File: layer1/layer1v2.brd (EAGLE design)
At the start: 17.8 x 48.3 mm, 15 parts, among them U1 microSD, U2 DS3234, U3 MMA8452Q

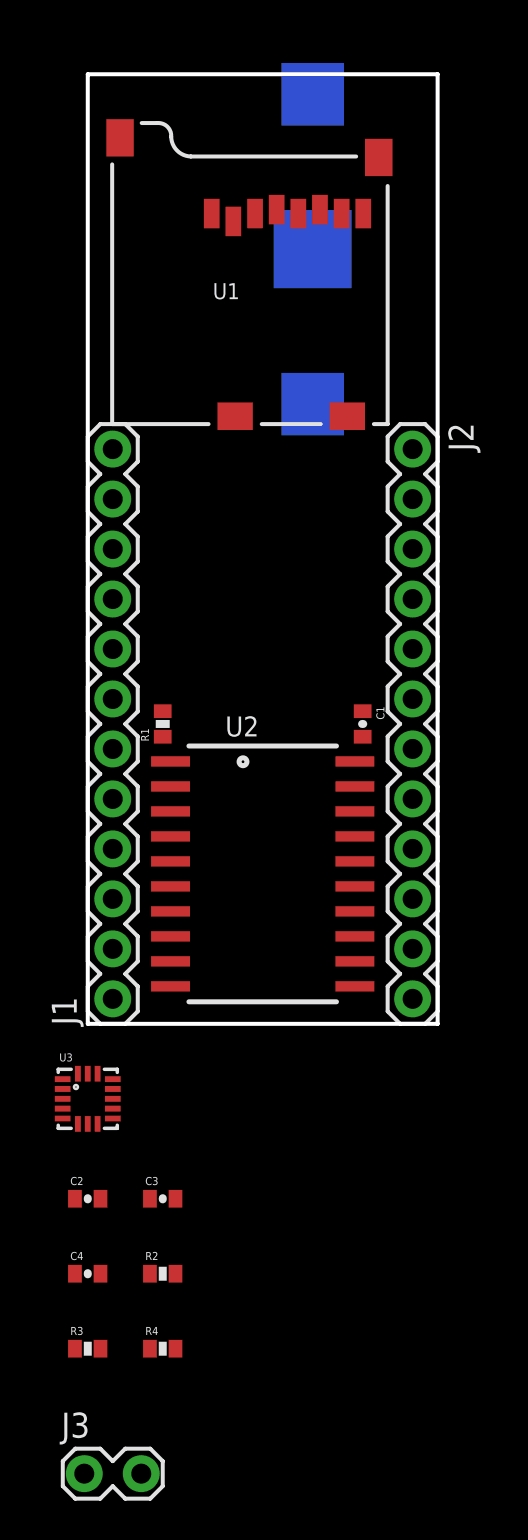
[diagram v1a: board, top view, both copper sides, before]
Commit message: removed battery, add accel
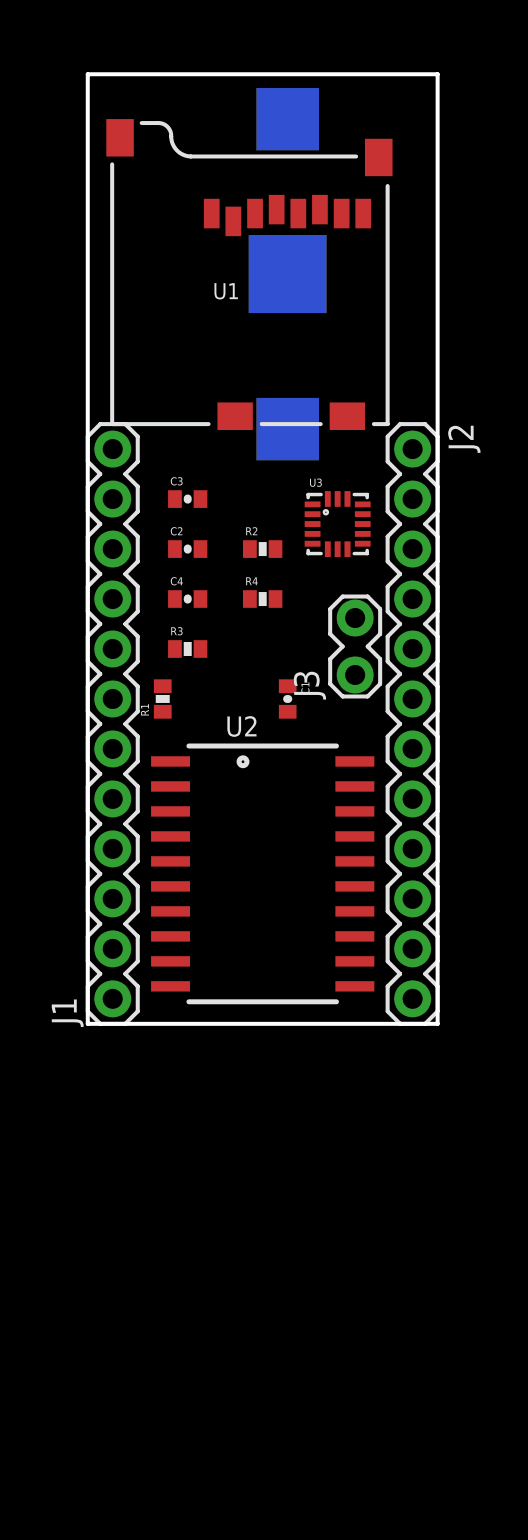
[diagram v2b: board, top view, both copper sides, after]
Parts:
- moved J3 43.0 mm to (13.6, 17.9), turned to 90 degrees
- moved R4 38.4 mm to (8.89, 21.6)
- moved R2 37.2 mm to (8.89, 24.1)
- moved R3 35.9 mm to (5.08, 19.1)
- moved C3 35.6 mm to (5.08, 26.7)
- moved C4 34.7 mm to (5.08, 21.6)
- moved C2 33.4 mm to (5.08, 24.1)
- moved U3 31.9 mm to (12.7, 25.4)
- moved C1 4.02 mm to (10.2, 16.5)
- moved BAT1 1.80 mm to (10.2, 38.1)
- moved R1 1.27 mm to (3.81, 16.5)
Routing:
- added copper zone on layer 16, net GND
- removed copper zone on layer 16, net N$1
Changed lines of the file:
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@@
 </autorouter>
 <elements>
-<element name="BAT1" library="SparkFun" package="BATTCON_12MM_CURVED" value="3V" x="11.43" y="39.37" rot="MR90"/>
-<element name="C1" library="SparkFun" package="0402-CAP" value="22pF" x="13.97" y="15.24" rot="R270"/>
-<element name="R1" library="SparkFun" package="0402-RES" value="10k" x="3.81" y="15.24" rot="R90"/>
+<element name="BAT1" library="SparkFun" package="BATTCON_12MM_CURVED" value="3V" x="10.16" y="38.1" rot="MR90"/>
+<element name="C1" library="SparkFun" package="0402-CAP" value="22pF" x="10.16" y="16.51" rot="R270"/>
+<element name="R1" library="SparkFun" package="0402-RES" value="10k" x="3.81" y="16.51" rot="R90"/>
 <element name="U1" library="SparkFun" package="MICRO-SD-SOCKET-PP" value="microSD" x="15.24" y="30.48"/>
 <element name="U2" library="SparkFun" package="DS3234" value="DS3234" x="8.89" y="7.62" rot="R270"/>
 <element name="J1" library="SparkFun-Connectors" package="1X12" value="" x="1.27" y="1.27" rot="R90"/>
 <element name="J2" library="SparkFun-Connectors" package="1X12" value="" x="16.51" y="29.21" rot="R270"/>
-<element name="U3" library="SparkFun" package="QFN-16_0.5MM" value="MMA8452Q" x="0" y="-3.81"/>
-<element name="C2" library="SparkFun" package="0402-CAP" value="0.1uF" x="0" y="-8.89"/>
-<element name="C3" library="SparkFun" package="0402-CAP" value="0.1uF" x="3.81" y="-8.89"/>
-<element name="C4" library="SparkFun" package="0402-CAP" value="4.7uF" x="0" y="-12.7"/>
-<element name="R2" library="SparkFun" package="0402-RES" value="10k" x="3.81" y="-12.7"/>
-<element name="R3" library="SparkFun" package="0402-RES" value="10k" x="0" y="-16.51"/>
-<element name="R4" library="SparkFun" package="0402-RES" value="10k" x="3.81" y="-16.51"/>
-<element name="J3" library="SparkFun-Connectors" package="1X02_LOCK" value="" x="0" y="-22.86"/>
+<element name="U3" library="SparkFun" package="QFN-16_0.5MM" value="MMA8452Q" x="12.7" y="25.4"/>
+<element name="C2" library="SparkFun" package="0402-CAP" value="0.1uF" x="5.08" y="24.13"/>
+<element name="C3" library="SparkFun" package="0402-CAP" value="0.1uF" x="5.08" y="26.67"/>
+<element name="C4" library="SparkFun" package="0402-CAP" value="4.7uF" x="5.08" y="21.59"/>
+<element name="R2" library="SparkFun" package="0402-RES" value="10k" x="8.89" y="24.13"/>
+<element name="R3" library="SparkFun" package="0402-RES" value="10k" x="5.08" y="19.05"/>
+<element name="R4" library="SparkFun" package="0402-RES" value="10k" x="8.89" y="21.59"/>
+<element name="J3" library="SparkFun-Connectors" package="1X02_LOCK" value="" x="13.589" y="17.907" rot="R90"/>
 </elements>
 <signals>
@@
 <contactref element="R4" pad="2"/>
 <wire x1="4.205" y1="9.525" x2="9.6" y2="41.38" width="0" layer="19" extent="1-1"/>
-<wire x1="3.81" y1="14.59" x2="4.205" y2="9.525" width="0" layer="19" extent="1-1"/>
-<wire x1="13.97" y1="14.59" x2="3.81" y2="14.59" width="0" layer="19" extent="1-1"/>
-<wire x1="16.51" y1="21.59" x2="13.97" y2="14.59" width="0" layer="19" extent="1-1"/>
-<wire x1="0.5" y1="-2.535" x2="3.81" y2="14.59" width="0" layer="19" extent="1-1"/>
-<wire x1="-1.275" y1="-2.81" x2="0.5" y2="-2.535" width="0" layer="19" extent="1-1"/>
-<wire x1="-0.65" y1="-8.89" x2="-1.275" y2="-2.81" width="0" layer="19" extent="1-1"/>
-<wire x1="-0.65" y1="-12.7" x2="-0.65" y2="-8.89" width="0" layer="19" extent="1-1"/>
-<wire x1="0.65" y1="-16.51" x2="-0.65" y2="-12.7" width="0" layer="19" extent="1-1"/>
-<wire x1="4.46" y1="-16.51" x2="0.65" y2="-16.51" width="0" layer="19" extent="1-1"/>
-<wire x1="4.46" y1="-12.7" x2="4.46" y2="-16.51" width="0" layer="19" extent="1-1"/>
+<wire x1="3.81" y1="15.86" x2="4.205" y2="9.525" width="0" layer="19" extent="1-1"/>
+<wire x1="10.16" y1="15.86" x2="3.81" y2="15.86" width="0" layer="19" extent="1-1"/>
+<wire x1="16.51" y1="21.59" x2="10.16" y2="15.86" width="0" layer="19" extent="1-1"/>
+<wire x1="13.2" y1="26.675" x2="3.81" y2="15.86" width="0" layer="19" extent="1-1"/>
+<wire x1="11.425" y1="26.4" x2="13.2" y2="26.675" width="0" layer="19" extent="1-1"/>
+<wire x1="4.43" y1="24.13" x2="11.425" y2="26.4" width="0" layer="19" extent="1-1"/>
+<wire x1="4.43" y1="21.59" x2="4.43" y2="24.13" width="0" layer="19" extent="1-1"/>
+<wire x1="5.73" y1="19.05" x2="4.43" y2="21.59" width="0" layer="19" extent="1-1"/>
+<wire x1="9.54" y1="21.59" x2="5.73" y2="19.05" width="0" layer="19" extent="1-1"/>
+<wire x1="9.54" y1="24.13" x2="9.54" y2="21.59" width="0" layer="19" extent="1-1"/>
 </signal>
 <signal name="GND">
@@
 <contactref element="C3" pad="2"/>
 <wire x1="11.8" y1="41.38" x2="14.79" y2="44.03" width="0" layer="19" extent="1-1"/>
-<wire x1="11.43" y1="39.37" x2="11.8" y2="41.38" width="0" layer="19" extent="1-16"/>
+<wire x1="10.16" y1="38.1" x2="11.8" y2="41.38" width="0" layer="19" extent="1-16"/>
 <wire x1="1.64" y1="45.03" x2="11.8" y2="41.38" width="0" layer="19" extent="1-1"/>
-<wire x1="16.51" y1="26.67" x2="11.43" y2="39.37" width="0" layer="19" extent="16-16"/>
+<wire x1="16.51" y1="26.67" x2="10.16" y2="38.1" width="0" layer="19" extent="16-16"/>
 <wire x1="13.575" y1="6.985" x2="16.51" y2="26.67" width="0" layer="19" extent="1-1"/>
 <wire x1="13.575" y1="5.715" x2="13.575" y2="6.985" width="0" layer="19" extent="1-1"/>
@@
 <wire x1="13.575" y1="3.175" x2="13.575" y2="4.445" width="0" layer="19" extent="1-1"/>
 <wire x1="13.575" y1="1.905" x2="13.575" y2="3.175" width="0" layer="19" extent="1-1"/>
-<wire x1="13.97" y1="15.89" x2="13.575" y2="1.905" width="0" layer="19" extent="1-1"/>
+<wire x1="10.16" y1="17.16" x2="13.575" y2="1.905" width="0" layer="19" extent="1-1"/>
 <wire x1="4.205" y1="5.715" x2="13.575" y2="5.715" width="0" layer="19" extent="1-1"/>
 <wire x1="4.205" y1="4.445" x2="4.205" y2="5.715" width="0" layer="19" extent="1-1"/>
@@
 <wire x1="1.27" y1="21.59" x2="4.205" y2="5.715" width="0" layer="19" extent="1-1"/>
 <wire x1="4.205" y1="12.065" x2="4.205" y2="5.715" width="0" layer="19" extent="1-1"/>
-<wire x1="1.275" y1="-3.31" x2="4.205" y2="1.905" width="0" layer="19" extent="1-1"/>
-<wire x1="1.275" y1="-4.31" x2="1.275" y2="-3.31" width="0" layer="19" extent="1-1"/>
-<wire x1="-1.275" y1="-4.81" x2="1.275" y2="-4.31" width="0" layer="19" extent="1-1"/>
-<wire x1="0.65" y1="-8.89" x2="-1.275" y2="-4.81" width="0" layer="19" extent="1-1"/>
-<wire x1="0.65" y1="-12.7" x2="0.65" y2="-8.89" width="0" layer="19" extent="1-1"/>
-<wire x1="4.46" y1="-8.89" x2="0.65" y2="-8.89" width="0" layer="19" extent="1-1"/>
+<wire x1="13.975" y1="25.9" x2="4.205" y2="1.905" width="0" layer="19" extent="1-1"/>
+<wire x1="13.975" y1="24.9" x2="13.975" y2="25.9" width="0" layer="19" extent="1-1"/>
+<wire x1="11.425" y1="24.4" x2="13.975" y2="24.9" width="0" layer="19" extent="1-1"/>
+<wire x1="5.73" y1="24.13" x2="11.425" y2="24.4" width="0" layer="19" extent="1-1"/>
+<wire x1="5.73" y1="21.59" x2="5.73" y2="24.13" width="0" layer="19" extent="1-1"/>
+<wire x1="5.73" y1="26.67" x2="5.73" y2="24.13" width="0" layer="19" extent="1-1"/>
+<polygon width="0.2032" layer="16">
+<vertex x="0" y="48.26"/>
+<vertex x="17.78" y="48.26"/>
+<vertex x="17.78" y="0"/>
+<vertex x="0" y="0"/>
+</polygon>
 </signal>
 <signal name="MISO">
@@
 <contactref element="U2" pad="5"/>
 <contactref element="J1" pad="8"/>
-<wire x1="4.205" y1="8.255" x2="3.81" y2="15.89" width="0" layer="19" extent="1-1"/>
+<wire x1="4.205" y1="8.255" x2="3.81" y2="17.16" width="0" layer="19" extent="1-1"/>
 <wire x1="1.27" y1="19.05" x2="4.205" y2="8.255" width="0" layer="19" extent="1-1"/>
 </signal>
@@
 <contactref element="U2" pad="16"/>
 <contactref element="BAT1" pad="PWR@1"/>
-<wire x1="11.43" y1="31.496" x2="13.575" y2="8.255" width="0" layer="19" extent="1-1"/>
+<wire x1="10.16" y1="30.226" x2="13.575" y2="8.255" width="0" layer="19" extent="1-1"/>
 </signal>
 <signal name="SD_CS">
@@
 <contactref element="J2" pad="1"/>
 </signal>
-<signal name="N$1">
-<polygon width="0.2032" layer="16">
-<vertex x="0" y="48.26"/>
-<vertex x="17.78" y="48.26"/>
-<vertex x="17.78" y="0"/>
-<vertex x="0" y="0"/>
-</polygon>
-</signal>
 <signal name="BYP">
 <contactref element="U3" pad="2"/>
 <contactref element="C3" pad="1"/>
-<wire x1="-1.275" y1="-3.31" x2="3.16" y2="-8.89" width="0" layer="19" extent="1-1"/>
+<wire x1="11.425" y1="25.9" x2="4.43" y2="26.67" width="0" layer="19" extent="1-1"/>
 </signal>
 <signal name="SCL">
@@
 <contactref element="R2" pad="1"/>
 <contactref element="J3" pad="2"/>
-<wire x1="3.16" y1="-12.7" x2="2.7178" y2="-22.86" width="0" layer="19" extent="1-1"/>
-<wire x1="-1.275" y1="-4.31" x2="3.16" y2="-12.7" width="0" layer="19" extent="1-1"/>
+<wire x1="8.24" y1="24.13" x2="13.589" y2="20.6248" width="0" layer="19" extent="1-1"/>
+<wire x1="11.425" y1="24.9" x2="8.24" y2="24.13" width="0" layer="19" extent="1-1"/>
 </signal>
 <signal name="SDA">
@@
 <contactref element="R3" pad="1"/>
 <contactref element="J3" pad="1"/>
-<wire x1="-0.65" y1="-16.51" x2="-0.1778" y2="-22.86" width="0" layer="19" extent="1-1"/>
-<wire x1="-0.5" y1="-5.085" x2="-0.65" y2="-16.51" width="0" layer="19" extent="1-1"/>
+<wire x1="4.43" y1="19.05" x2="13.589" y2="17.7292" width="0" layer="19" extent="1-1"/>
+<wire x1="12.2" y1="24.125" x2="4.43" y2="19.05" width="0" layer="19" extent="1-1"/>
 </signal>
 <signal name="SA0">
 <contactref element="U3" pad="7"/>
 <contactref element="R4" pad="1"/>
-<wire x1="0" y1="-5.085" x2="3.16" y2="-16.51" width="0" layer="19" extent="1-1"/>
+<wire x1="12.7" y1="24.125" x2="8.24" y2="21.59" width="0" layer="19" extent="1-1"/>
 </signal>
 </signals>

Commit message: who needs commits
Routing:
- net GND: track 0.00 -> 0.80 mm
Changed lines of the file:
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@@
 <wire x1="1.27" y1="21.59" x2="4.205" y2="5.715" width="0" layer="19" extent="1-1"/>
 <wire x1="4.205" y1="12.065" x2="4.205" y2="5.715" width="0" layer="19" extent="1-1"/>
-<wire x1="13.975" y1="25.9" x2="4.205" y2="1.905" width="0" layer="19" extent="1-1"/>
 <wire x1="13.975" y1="24.9" x2="13.975" y2="25.9" width="0" layer="19" extent="1-1"/>
 <wire x1="11.425" y1="24.4" x2="13.975" y2="24.9" width="0" layer="19" extent="1-1"/>
@@
 <vertex x="0" y="0"/>
 </polygon>
+<wire x1="4.205" y1="1.905" x2="4.205" y2="1.665" width="0.4064" layer="1"/>
+<wire x1="4.205" y1="1.665" x2="3.81" y2="1.27" width="0.4064" layer="1"/>
+<wire x1="3.81" y1="1.27" x2="4.205" y2="3.175" width="0" layer="19" extent="1-16"/>
 </signal>
 <signal name="MISO">

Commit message: ops
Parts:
- moved C1 25.9 mm to (5.08, 41.9), turned to 0 degrees
- moved R3 25.3 mm to (12.7, 43.2), turned to 180 degrees
- moved BAT1 24.2 mm to (8.89, 14.0)
- moved R4 21.6 mm to (7.62, 43.2), turned to 270 degrees
- moved C4 21.6 mm to (5.08, 43.2), turned to 180 degrees
- moved C2 20.3 mm to (5.08, 44.5), turned to 180 degrees
- moved U2 20.3 mm to (8.89, 27.9)
- moved U3 20.3 mm to (12.7, 45.7)
- moved J1 19.1 mm to (1.27, 20.3)
- moved J3 19.1 mm to (13.6, 37.0)
- moved R2 19.1 mm to (8.89, 43.2), turned to 270 degrees
- moved C3 19.0 mm to (5.08, 45.7), turned to 180 degrees
- moved J2 19.0 mm to (16.5, 48.3)
- moved U1 18.0 mm to (2.54, 17.8), turned to 180 degrees
- moved R1 4.58 mm to (7.62, 19.1), turned to 180 degrees
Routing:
- net VCC: track 0.00 -> 67.4 mm, vias 0 -> 3
- net GND: track 0.80 -> 45.9 mm, vias 0 -> 5
- net VBATT: track 0.00 -> 28.4 mm, vias 0 -> 1
- net MOSI: track 0.00 -> 18.5 mm
- net SD_CS: track 0.00 -> 18.1 mm
- net BYP: track 0.00 -> 11.3 mm
- net INT/SQW: track 0.00 -> 10.8 mm
- net SDA: track 0.00 -> 9.61 mm
- net SCL: track 0.00 -> 9.53 mm
- net SA0: track 0.00 -> 7.50 mm
- net SCK: track 0.00 -> 7.36 mm
- net N$1: track 0.00 -> 4.34 mm
- removed copper zone on layer 16, net GND
